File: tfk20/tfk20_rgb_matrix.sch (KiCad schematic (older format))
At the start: 37 parts, among them U4 IS31FL3733-TQ

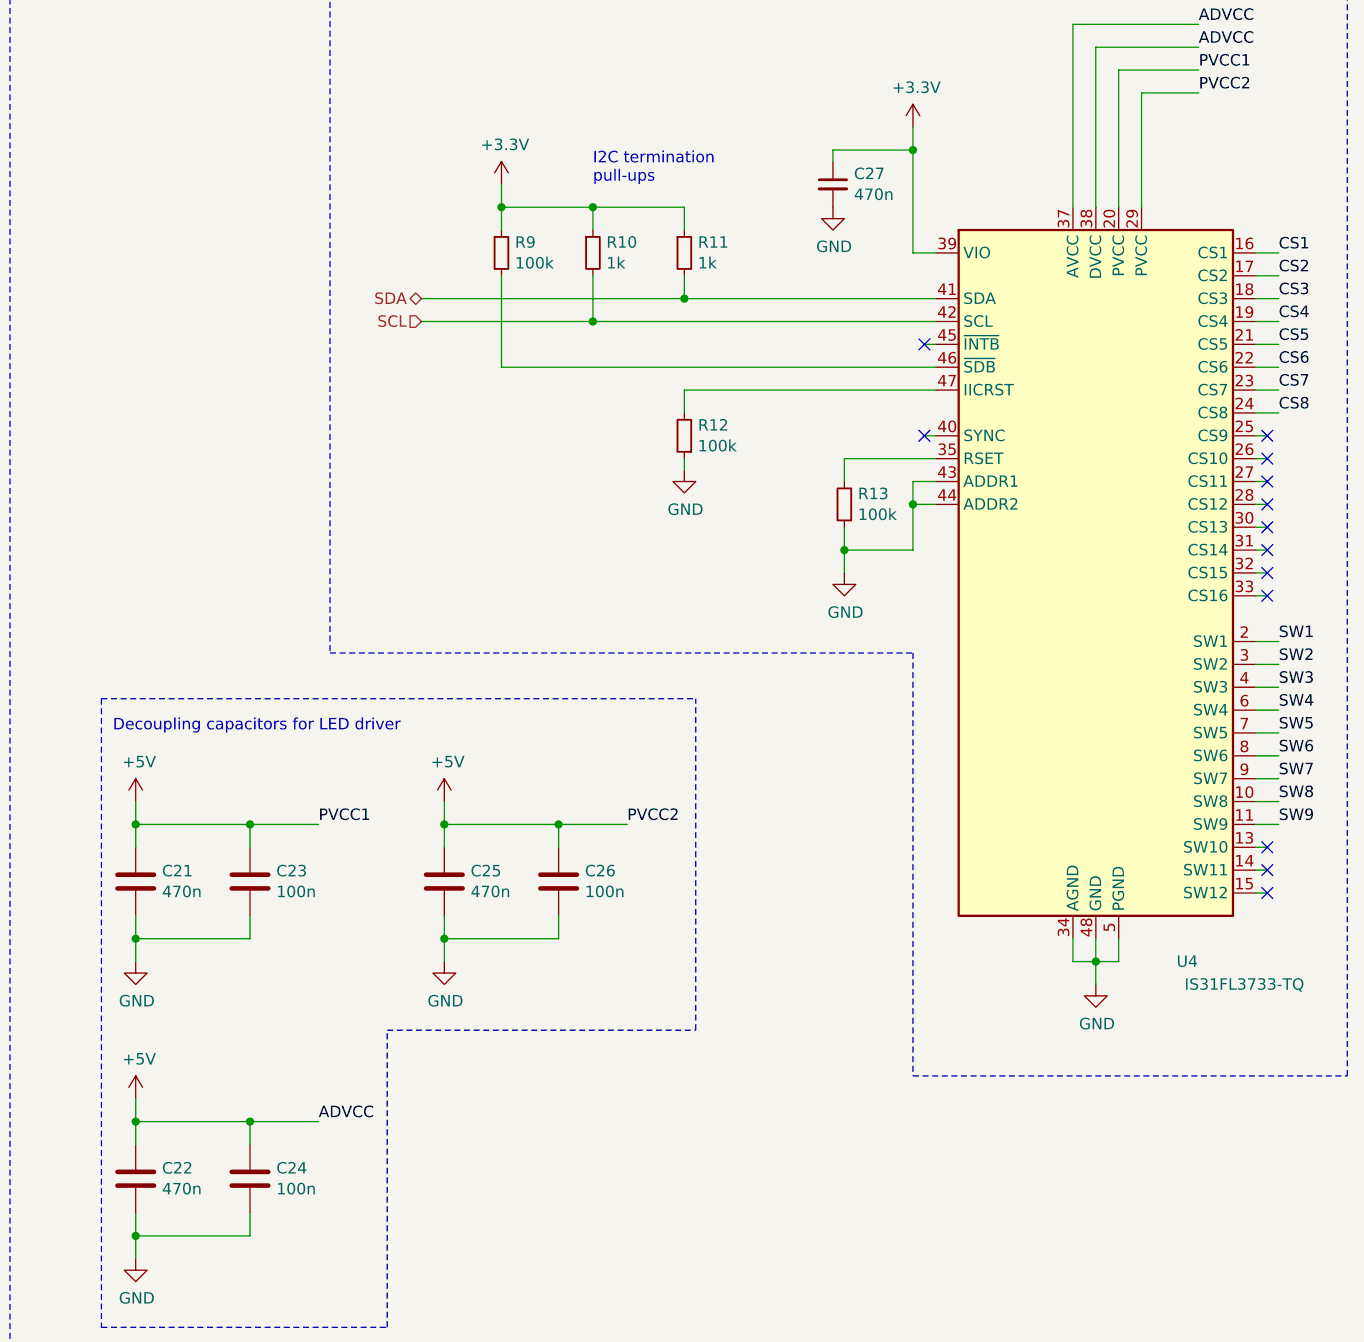
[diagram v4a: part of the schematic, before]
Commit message: Implement sophisticated USB-C protection
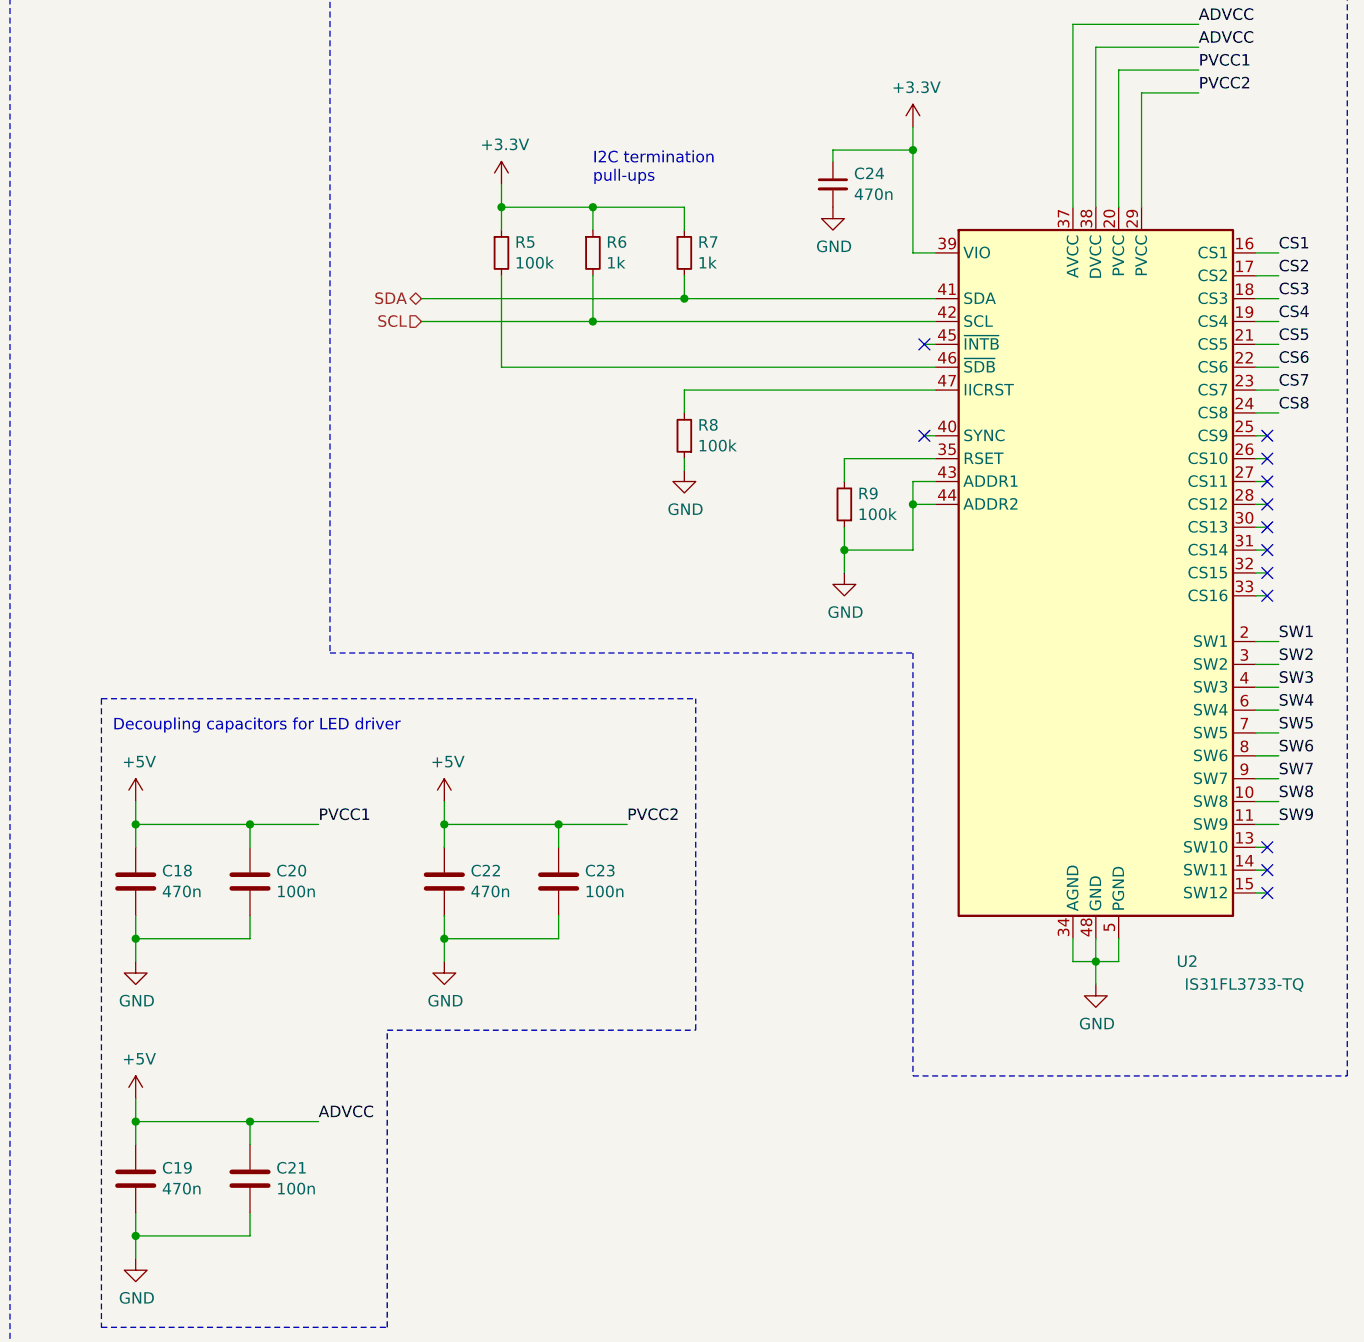
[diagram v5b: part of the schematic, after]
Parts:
- renumbered C21 to C18, C22 to C19, C23 to C20, C24 to C21, C25 to C22, C26 to C23, C27 to C24, R9 to R5, R10 to R6, R11 to R7, R12 to R8, R13 to R9, U4 to U2
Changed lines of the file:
@@
 $Descr A4 11693 8268
 encoding utf-8
-Sheet 4 4
+Sheet 4 5
 Title "tfk20"
 Date "2021-02-02"
@@
 	9150 1950 9250 1950
 $Comp
-L power:+3.3V #PWR060
+L power:+3.3V #PWR048
 U 1 1 60214F18
 P 9150 1400
-F 0 "#PWR060" H 9150 1250 50  0001 C CNN
+F 0 "#PWR048" H 9150 1250 50  0001 C CNN
 F 1 "+3.3V" H 9165 1573 50  0000 C CNN
 F 2 "" H 9150 1400 50  0001 C CNN
@@
 $EndComp
 $Comp
-L Device:C_Small C27
+L Device:C_Small C24
 U 1 1 602157F1
 P 8800 1650
-F 0 "C27" H 8892 1696 50  0000 L CNN
+F 0 "C24" H 8892 1696 50  0000 L CNN
 F 1 "470n" H 8892 1605 50  0000 L CNN
 F 2 "" H 8800 1650 50  0001 C CNN
@@
 	8150 2550 8150 2650
 $Comp
-L Device:R_Small R12
+L Device:R_Small R8
 U 1 1 6021C88C
 P 8150 2750
-F 0 "R12" H 8091 2704 50  0000 R CNN
+F 0 "R8" H 8091 2704 50  0000 R CNN
 F 1 "100k" H 8091 2795 50  0000 R CNN
 F 2 "" H 8150 2750 50  0001 C CNN
@@
 	8150 2850 8150 2900
 $Comp
-L power:GND #PWR057
+L power:GND #PWR045
 U 1 1 6021F1B8
 P 8150 2900
-F 0 "#PWR057" H 8150 2650 50  0001 C CNN
+F 0 "#PWR045" H 8150 2650 50  0001 C CNN
 F 1 "GND" H 8155 2727 50  0000 C CNN
 F 2 "" H 8150 2900 50  0001 C CNN
@@
 $EndComp
 $Comp
-L Device:R_Small R9
+L Device:R_Small R5
 U 1 1 60220F15
 P 7350 1950
-F 0 "R9" H 7409 1996 50  0000 L CNN
+F 0 "R5" H 7409 1996 50  0000 L CNN
 F 1 "100k" H 7409 1905 50  0000 L CNN
 F 2 "" H 7350 1950 50  0001 C CNN
@@
 $EndComp
 $Comp
-L Device:R_Small R10
+L Device:R_Small R6
 U 1 1 602213A8
 P 7750 1950
-F 0 "R10" H 7809 1996 50  0000 L CNN
+F 0 "R6" H 7809 1996 50  0000 L CNN
 F 1 "1k" H 7809 1905 50  0000 L CNN
 F 2 "" H 7750 1950 50  0001 C CNN
@@
 $EndComp
 $Comp
-L Device:R_Small R11
+L Device:R_Small R7
 U 1 1 60221B5F
 P 8150 1950
-F 0 "R11" H 8209 1996 50  0000 L CNN
+F 0 "R7" H 8209 1996 50  0000 L CNN
 F 1 "1k" H 8209 1905 50  0000 L CNN
 F 2 "" H 8150 1950 50  0001 C CNN
@@
 Connection ~ 7350 1750
 $Comp
-L power:+3.3V #PWR056
+L power:+3.3V #PWR044
 U 1 1 602234A9
 P 7350 1650
-F 0 "#PWR056" H 7350 1500 50  0001 C CNN
+F 0 "#PWR044" H 7350 1500 50  0001 C CNN
 F 1 "+3.3V" H 7365 1823 50  0000 C CNN
 F 2 "" H 7350 1650 50  0001 C CNN
@@
 	8850 2850 8850 2950
 $Comp
-L Device:R_Small R13
+L Device:R_Small R9
 U 1 1 60228ACD
 P 8850 3050
-F 0 "R13" H 8791 3004 50  0000 R CNN
+F 0 "R9" H 8791 3004 50  0000 R CNN
 F 1 "100k" H 8791 3095 50  0000 R CNN
 F 2 "" H 8850 3050 50  0001 C CNN
@@
 	8850 3250 8850 3350
 $Comp
-L power:GND #PWR059
+L power:GND #PWR047
 U 1 1 6022B57B
 P 8850 3350
-F 0 "#PWR059" H 8850 3100 50  0001 C CNN
+F 0 "#PWR047" H 8850 3100 50  0001 C CNN
 F 1 "GND" H 8855 3177 50  0000 C CNN
 F 2 "" H 8850 3350 50  0001 C CNN
@@
 $EndComp
 $Comp
-L Driver_LED:IS31FL3733-TQ U4
+L Driver_LED:IS31FL3733-TQ U2
 U 1 1 602119B1
 P 9950 3350
-F 0 "U4" H 10350 1650 50  0000 C CNN
+F 0 "U2" H 10350 1650 50  0000 C CNN
 F 1 "IS31FL3733-TQ" H 10600 1550 50  0000 C CNN
 F 2 "Package_QFP:TQFP-48-1EP_7x7mm_P0.5mm_EP5x5mm" H 9950 3350 50  0001 C CNN
@@
 	9950 5050 9950 5150
 $Comp
-L Device:C C21
+L Device:C C18
 U 1 1 60233B22
 P 5750 4700
-F 0 "C21" H 5865 4746 50  0000 L CNN
+F 0 "C18" H 5865 4746 50  0000 L CNN
 F 1 "470n" H 5865 4655 50  0000 L CNN
 F 2 "" H 5788 4550 50  0001 C CNN
@@
 $EndComp
 $Comp
-L Device:C C23
+L Device:C C20
 U 1 1 60234E7C
 P 6250 4700
-F 0 "C23" H 6365 4746 50  0000 L CNN
+F 0 "C20" H 6365 4746 50  0000 L CNN
 F 1 "100n" H 6365 4655 50  0000 L CNN
 F 2 "" H 6288 4550 50  0001 C CNN
@@
 Connection ~ 5750 4450
 $Comp
-L power:+5V #PWR050
+L power:+5V #PWR038
 U 1 1 6023A005
 P 5750 4350
-F 0 "#PWR050" H 5750 4200 50  0001 C CNN
+F 0 "#PWR038" H 5750 4200 50  0001 C CNN
 F 1 "+5V" H 5765 4523 50  0000 C CNN
 F 2 "" H 5750 4350 50  0001 C CNN
@@
 PVCC1
 $Comp
-L Device:C C25
+L Device:C C22
 U 1 1 6023CACA
 P 7100 4700
-F 0 "C25" H 7215 4746 50  0000 L CNN
+F 0 "C22" H 7215 4746 50  0000 L CNN
 F 1 "470n" H 7215 4655 50  0000 L CNN
 F 2 "" H 7138 4550 50  0001 C CNN
@@
 $EndComp
 $Comp
-L Device:C C26
+L Device:C C23
 U 1 1 6023CAD0
 P 7600 4700
-F 0 "C26" H 7715 4746 50  0000 L CNN
+F 0 "C23" H 7715 4746 50  0000 L CNN
 F 1 "100n" H 7715 4655 50  0000 L CNN
 F 2 "" H 7638 4550 50  0001 C CNN
@@
 Connection ~ 7100 4450
 $Comp
-L power:+5V #PWR054
+L power:+5V #PWR042
 U 1 1 6023CAE3
 P 7100 4350
-F 0 "#PWR054" H 7100 4200 50  0001 C CNN
+F 0 "#PWR042" H 7100 4200 50  0001 C CNN
 F 1 "+5V" H 7115 4523 50  0000 C CNN
 F 2 "" H 7100 4350 50  0001 C CNN
@@
 $EndComp
 $Comp
-L power:GND #PWR055
+L power:GND #PWR043
 U 1 1 6023CAE9
 P 7100 5050
-F 0 "#PWR055" H 7100 4800 50  0001 C CNN
+F 0 "#PWR043" H 7100 4800 50  0001 C CNN
 F 1 "GND" H 7105 4877 50  0000 C CNN
 F 2 "" H 7100 5050 50  0001 C CNN
@@
 PVCC2
 $Comp
-L Device:C C22
+L Device:C C19
 U 1 1 6023EA0C
 P 5750 6000
-F 0 "C22" H 5865 6046 50  0000 L CNN
+F 0 "C19" H 5865 6046 50  0000 L CNN
 F 1 "470n" H 5865 5955 50  0000 L CNN
 F 2 "" H 5788 5850 50  0001 C CNN
@@
 $EndComp
 $Comp
-L Device:C C24
+L Device:C C21
 U 1 1 6023EA12
 P 6250 6000
-F 0 "C24" H 6135 5954 50  0000 R CNN
+F 0 "C21" H 6135 5954 50  0000 R CNN
 F 1 "100n" H 6135 6045 50  0000 R CNN
 F 2 "" H 6288 5850 50  0001 C CNN
@@
 Connection ~ 5750 5750
 $Comp
-L power:+5V #PWR052
+L power:+5V #PWR040
 U 1 1 6023EA25
 P 5750 5650
-F 0 "#PWR052" H 5750 5500 50  0001 C CNN
+F 0 "#PWR040" H 5750 5500 50  0001 C CNN
 F 1 "+5V" H 5765 5823 50  0000 C CNN
 F 2 "" H 5750 5650 50  0001 C CNN
@@
 $EndComp
 $Comp
-L power:GND #PWR053
+L power:GND #PWR041
 U 1 1 6023EA2B
 P 5750 6350
-F 0 "#PWR053" H 5750 6100 50  0001 C CNN
+F 0 "#PWR041" H 5750 6100 50  0001 C CNN
 F 1 "GND" H 5755 6177 50  0000 C CNN
 F 2 "" H 5750 6350 50  0001 C CNN
@@
 NoConn ~ 9200 2750
 $Comp
-L power:GND #PWR058
+L power:GND #PWR046
 U 1 1 606D7D2A
 P 8800 1750
-F 0 "#PWR058" H 8800 1500 50  0001 C CNN
+F 0 "#PWR046" H 8800 1500 50  0001 C CNN
 F 1 "GND" H 8805 1577 50  0000 C CNN
 F 2 "" H 8800 1750 50  0001 C CNN
@@
 $EndComp
 $Comp
-L power:GND #PWR051
+L power:GND #PWR039
 U 1 1 606D922B
 P 5750 5050
-F 0 "#PWR051" H 5750 4800 50  0001 C CNN
+F 0 "#PWR039" H 5750 4800 50  0001 C CNN
 F 1 "GND" H 5755 4877 50  0000 C CNN
 F 2 "" H 5750 5050 50  0001 C CNN
@@
 $EndComp
 $Comp
-L power:GND #PWR061
+L power:GND #PWR049
 U 1 1 606DA6F0
 P 9950 5150
-F 0 "#PWR061" H 9950 4900 50  0001 C CNN
+F 0 "#PWR049" H 9950 4900 50  0001 C CNN
 F 1 "GND" H 9955 4977 50  0000 C CNN
 F 2 "" H 9950 5150 50  0001 C CNN

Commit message: Add STL11N3LLH6 footprint
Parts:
- renumbered C18 to C401, C19 to C402, C20 to C403, C21 to C404, C22 to C405, C23 to C406, C24 to C407, D33 to D401, D34 to D402, D35 to D403, D36 to D404, D37 to D405, D38 to D406, D39 to D407, D40 to D408, D41 to D409, D42 to D410, D43 to D411, D44 to D412, D45 to D413, D46 to D414, D47 to D415, D48 to D416, D49 to D417, D50 to D418, D51 to D419, D52 to D420, D53 to D421, D54 to D422, D55 to D423, D56 to D424, R5 to R401, R6 to R402, R7 to R403, R8 to R404, R9 to R405, U2 to U401
